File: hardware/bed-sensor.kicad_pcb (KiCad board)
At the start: 2 copper layers, 21.9 x 43.2 mm, 49 parts, among them J1 USB_B_Mini, J2 Conn_ARM_JTAG_SWD_10, J3 DM3AT-SF-PEJM5, J4 Conn_01x02, Q1 Q_PMOS_GSD, SW1 SW_Push, U1 MCP73831-2-OT, U2 TLV70218_SOT23-5, U3 AP2112K-3.3, U4 MDBT50Q-1M, U5 PCA9306, U6 ICM-20948, U7 BMP280, Y1 32.768

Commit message: added bom file
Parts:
- R17, R18, R2: value 100k -> 100K
- R5: value 4.7k -> 4.7K
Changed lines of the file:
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@@
       (effects (font (size 0.6 0.6) (thickness 0.15)))
     )
-    (fp_text value 100k (at 0 1.43 180) (layer F.Fab)
+    (fp_text value 100K (at 0 1.43 180) (layer F.Fab)
       (effects (font (size 1 1) (thickness 0.15)))
     )
@@
       (effects (font (size 1 1) (thickness 0.15)))
     )
-    (fp_text value 4.7k (at 0 1.43 180) (layer F.Fab)
+    (fp_text value 4.7K (at 0 1.43 180) (layer F.Fab)
       (effects (font (size 1 1) (thickness 0.15)))
     )
@@
       (effects (font (size 0.5 0.5) (thickness 0.125)))
     )
-    (fp_text value 100k (at 0 1.43 90) (layer F.Fab)
+    (fp_text value 100K (at 0 1.43 90) (layer F.Fab)
       (effects (font (size 1 1) (thickness 0.15)))
     )
@@
       (effects (font (size 0.5 0.5) (thickness 0.125)))
     )
-    (fp_text value 100k (at 0 1.43) (layer F.Fab)
-      (effects (font (size 1 1) (thickness 0.15)))
-    )
+    (fp_text value 100K (at 0 1.43) (layer F.Fab)
+      (effects (font (size 1 1) (thickness 0.15)))
+    )

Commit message: updated csv
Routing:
- net Net-(C3-Pad1): track 23.4 -> 21.6 mm, vias 1 -> 0

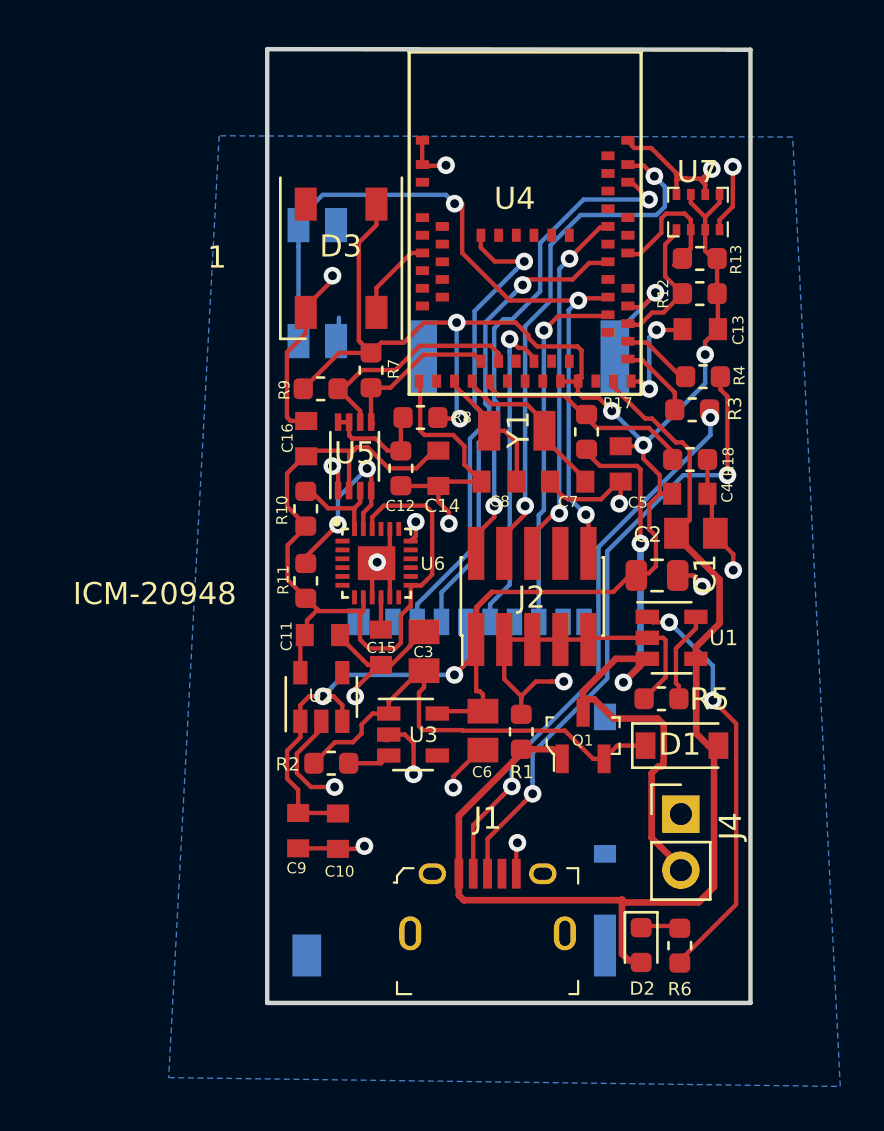
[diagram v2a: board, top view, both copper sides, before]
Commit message: rounded off corners
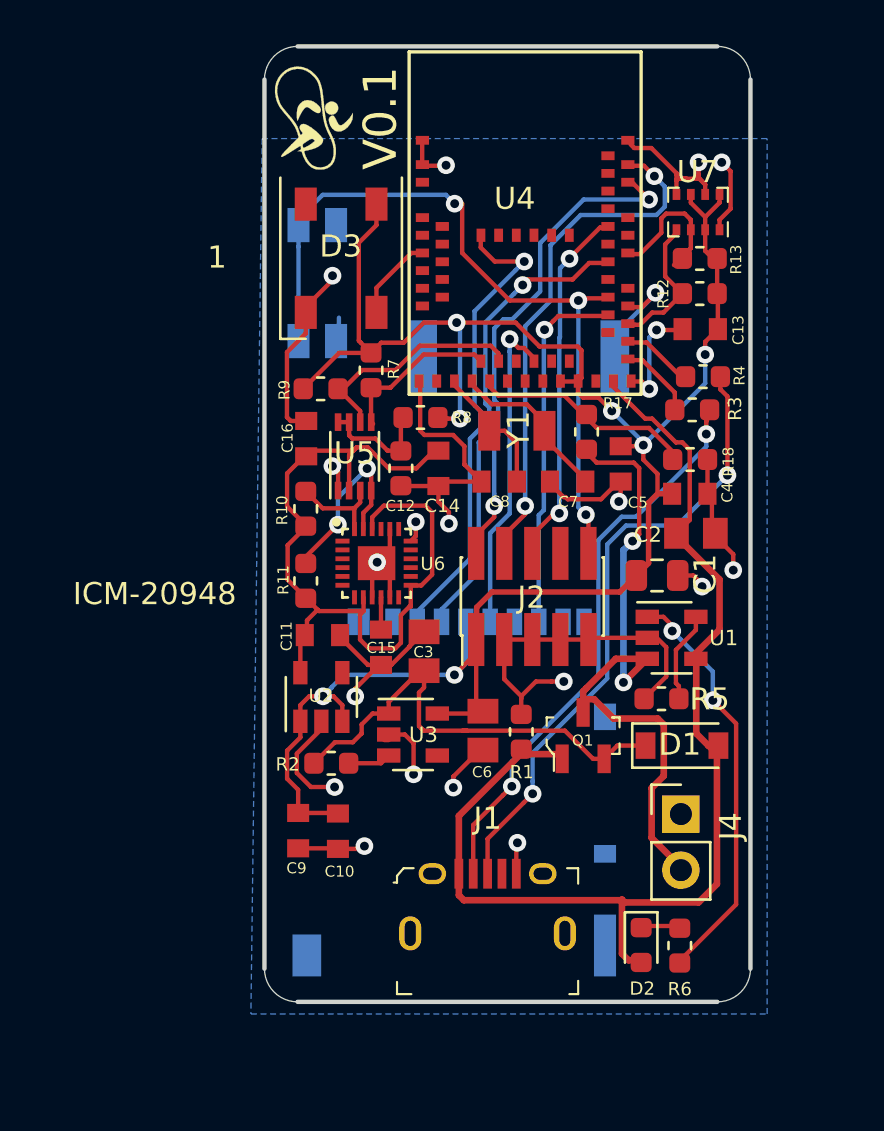
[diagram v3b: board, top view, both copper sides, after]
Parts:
- added G***: LOGO, extra:gait_logo, F.Cu at (138.5, 89.5)
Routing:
- net +3V3: track 96.0 -> 95.3 mm
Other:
- board size 21.9 x 43.2 mm -> 22 x 43.2 mm
- board text added: "V0.1"
